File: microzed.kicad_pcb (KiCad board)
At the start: 10 copper layers, 60 x 100 mm, 333 parts, among them IC1 XC7Z020-1CLG484C, IC2 RTL8211E-VL-CG, J1 640456-3, J2 10104111-0001LF, J3 L829-1J1T-43, J4 Micro_SD_Card_Det_Hirose_DM3AT, J5 10104111-0001LF, J6 BSH-090-01-X-D-A, J7 BSH-090-01-X-D-A, Q1 MMBT3904, Q2 MMBT3904, SW1 SW_Push, U1 TLV62130RGTR, U10 MT41K256M16TW, U11 MT25QL128ABA8E12-1SIT, U12 USB3320C-EZK, U13 ASDMB-24.000MHZ-LC-T, U14 ASDMB-25.000MHZ-LC-T, U15 TXS02612RTWR, U16 CP2104-F03-GM, U2 TLV62130RGTR, U3 TLV62130RGTR, U4 TLV62130RGTR, U5 TLV62130RGTR, U6 ASDMB-33.333MHZ-LC-T, U7 TPS51206DSQR, U8 REF3012, U9 MT41K256M16TW

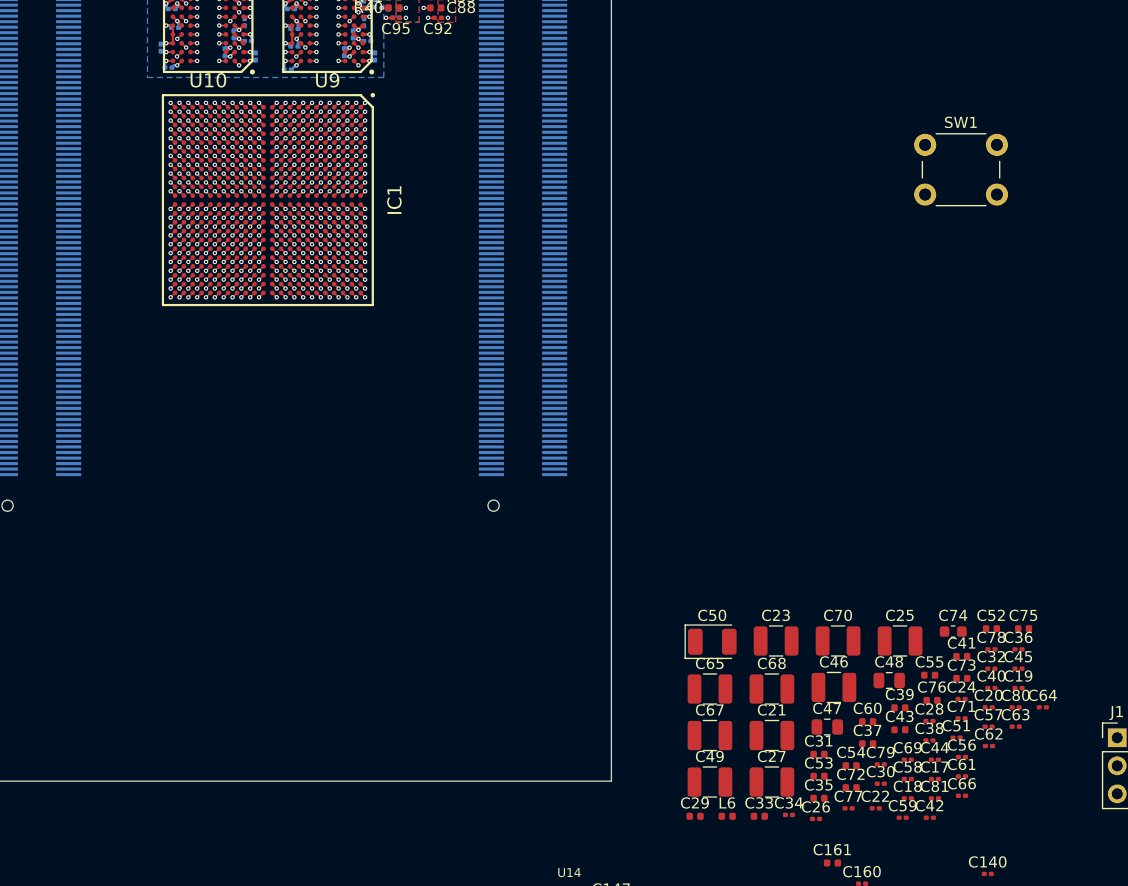
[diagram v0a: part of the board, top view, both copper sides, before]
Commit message: start zynq power capacitors
Signed-off-by: Yi Qingliang <niqingliang2003@gmail.com>
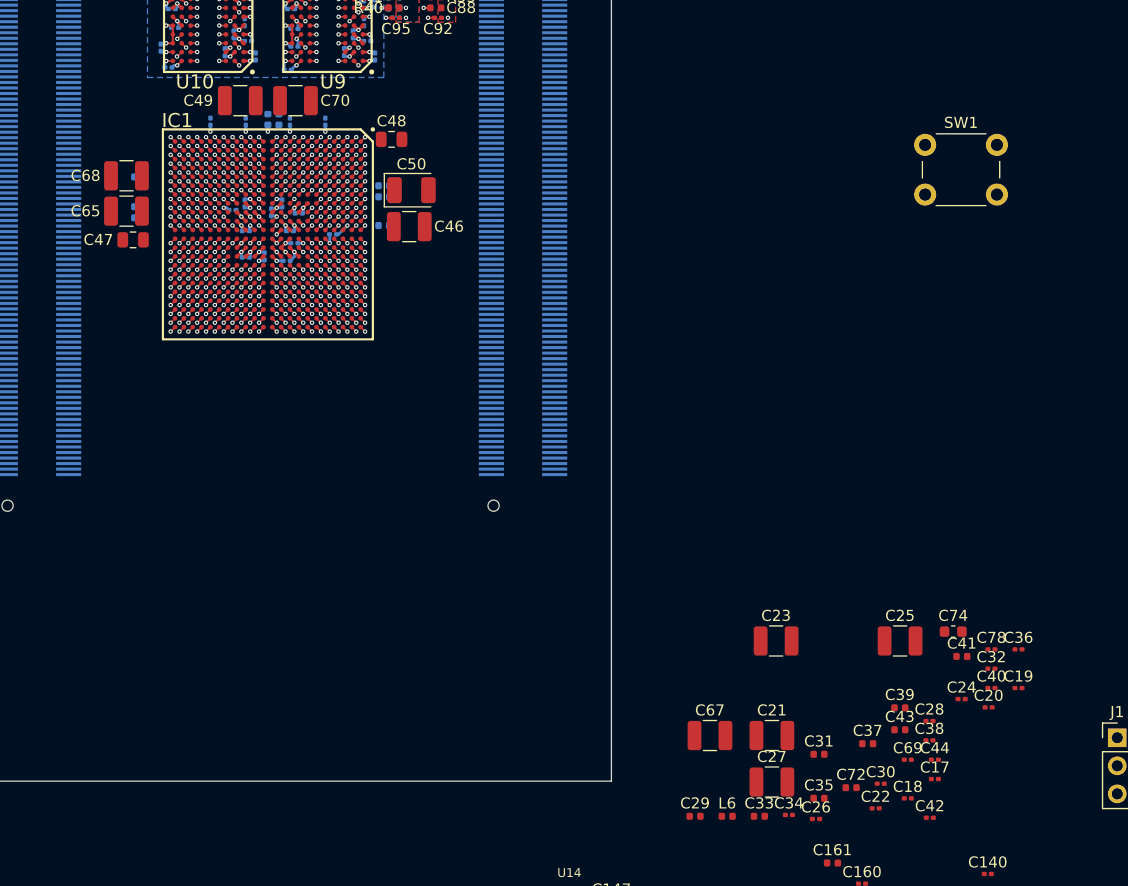
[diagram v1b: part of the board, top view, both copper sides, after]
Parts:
- C45, C51, C52, C53, C54, C55, C56, C57, C58, C59, C60, C61, C62, C63, C64, C66, C71, C73, C75, C76, C77, C79, C80, C81: moved to B.Cu
- moved C66 89.0 mm to (-3.10, 40.3), turned to 90 degrees
- moved C75 88.7 mm to (-12.7, 48.0), turned to 180 degrees
- moved C73 87.2 mm to (-12.7, 45.3), turned to 180 degrees
- moved C71 86.8 mm to (-6.30, 40.3), turned to 90 degrees
- moved C64 85.4 mm to (-3.20, 47.7), turned to 270 degrees
- moved C81 84.6 mm to (0.90, 40.3), turned to 90 degrees
- moved C80 84.0 mm to (-4.30, 48.3)
- moved C62 81.9 mm to (-3.10, 50.2)
- moved C63 81.6 mm to (0.20, 47.7), turned to 270 degrees
- moved C76 79.9 mm to (-1.10, 40.1), turned to 90 degrees
- moved C53 79.6 mm to (-12.7, 49.0), turned to 180 degrees
- moved C45 79.2 mm to (-3.10, 52.6)
- moved C77 78.2 mm to (4.10, 40.3), turned to 90 degrees
- moved C54 78.1 mm to (-0.10, 40.1), turned to 90 degrees
- moved C57 77.5 mm to (0.90, 50.2), turned to 180 degrees
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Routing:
- net GND: track 112.4 -> 120.2 mm, vias 173 -> 164
- net VCCBRAM: track 22.0 -> 26.9 mm, vias 23 -> 18
- net VCCO_DDR: track 63.6 -> 66.5 mm, vias 55 -> 60
- net PWR_B501: track 19.7 -> 22.1 mm, vias 20 -> 18
- net GNDADC: vias 2 -> 1

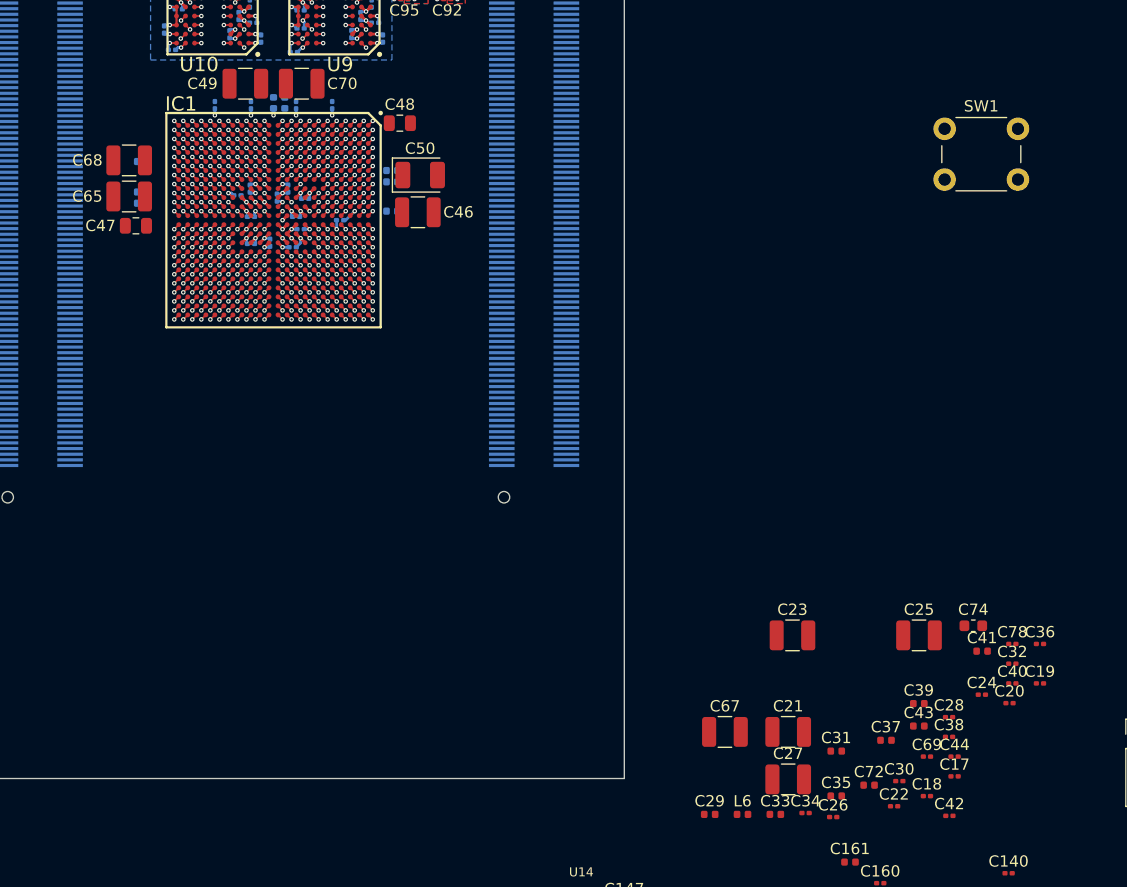
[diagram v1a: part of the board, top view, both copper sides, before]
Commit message: zynq power capacitors done. start power plane
Signed-off-by: Yi Qingliang <niqingliang2003@gmail.com>
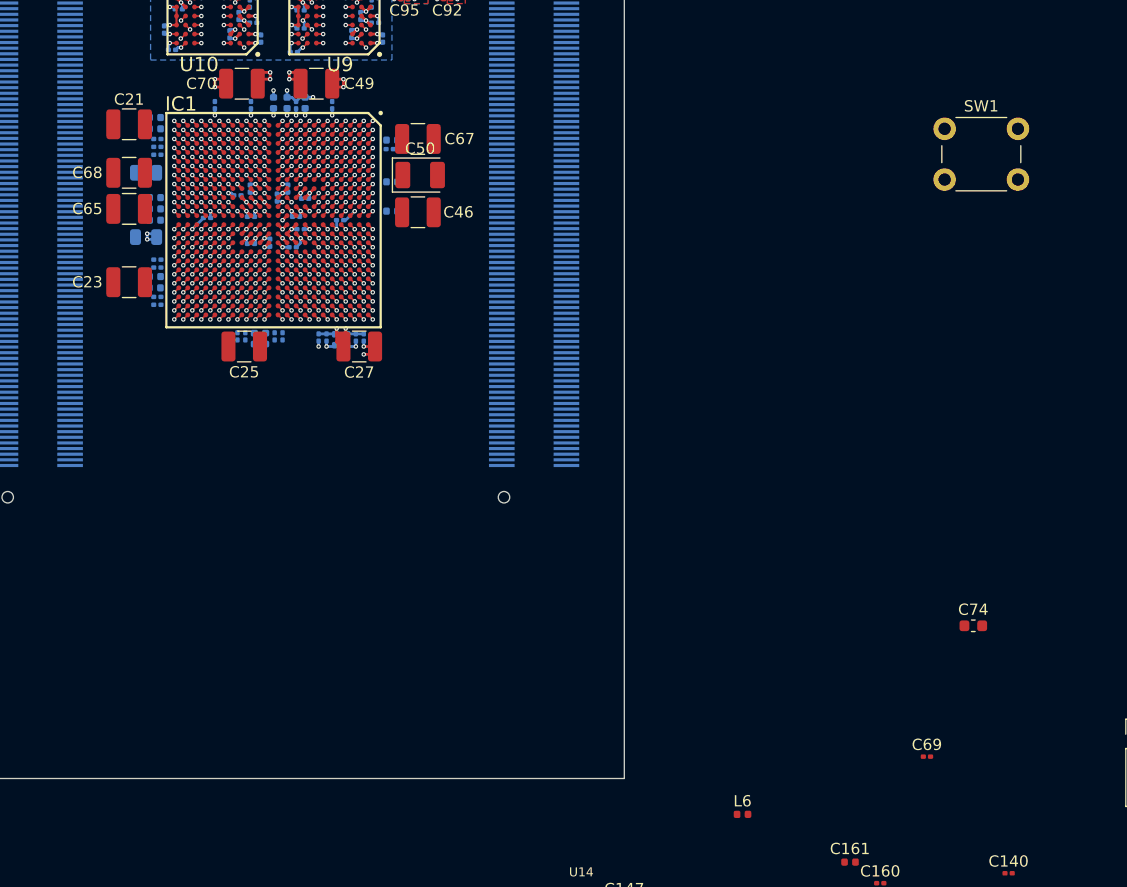
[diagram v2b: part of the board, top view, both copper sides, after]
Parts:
- C17, C18, C19, C20, C22, C24, C26, C28, C29, C30, C31, C32, C33, C34, C35, C36, C37, C38, C39, C40, C41, C42, C43, C44, C47, C48, C72, C78: moved to B.Cu
- moved C22 88.1 mm to (-11.4, 43.3), turned to 180 degrees
- moved C38 87.5 mm to (-11.4, 44.0), turned to 180 degrees
- moved C30 86.1 mm to (-11.4, 44.7), turned to 180 degrees
- moved C37 84.5 mm to (-11.6, 42.4), turned to 180 degrees
- moved C32 83.8 mm to (-11.4, 54.0), turned to 180 degrees
- moved C40 83.2 mm to (-11.4, 57.3), turned to 180 degrees
- moved C18 82.8 mm to (-11.4, 54.7), turned to 180 degrees
- moved C17 82.7 mm to (-7.00, 50.3), turned to 180 degrees
- moved C24 80.9 mm to (-11.4, 58.0), turned to 180 degrees
- moved C21 79.5 mm to (-13.9, 42.0), turned to 180 degrees
- moved C29 79.0 mm to (-11.6, 41.4), turned to 180 degrees
- moved C39 77.6 mm to (-11.6, 55.5), turned to 180 degrees
- moved C19 77.5 mm to (-4.30, 60.8), turned to 270 degrees
- moved C42 75.5 mm to (-3.60, 60.8), turned to 270 degrees
- moved C31 73.0 mm to (-11.6, 56.5), turned to 180 degrees
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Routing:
- net GND: track 120.2 -> 132.4 mm, vias 164 -> 176
- net VCCO_35: track 3.96 -> 12.8 mm, vias 7 -> 9
- net VCCO_DDR: track 66.5 -> 61.5 mm, vias 60 -> 62
- net VCCBRAM: track 26.9 -> 30.3 mm, vias 18 -> 22
- net V3V3: track 20.0 -> 22.4 mm, vias 18 -> 20
- net VCCO_13: track 3.96 -> 4.57 mm
- added copper zone on In5.Cu.GND, net PWR_B501
- added copper zone on In4.Cu.VDD, net V3V3
- added copper zone on In4.Cu.VDD, net VCCBRAM
- added copper zone on In4.Cu.VDD, net VCCO_13
- added copper zone on In4.Cu.VDD, net VCCO_33
- added copper zone on In4.Cu.VDD, net VCCO_34
- added copper zone on In4.Cu.VDD, net VCCO_35
